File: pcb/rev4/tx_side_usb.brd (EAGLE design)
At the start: 28 x 36.5 mm, 55 parts, among them Q1 BSS84, U3 MCP73831T-2ACI/OT, Y1 CRYSTAL-26MHZSMD-3.2X2.5

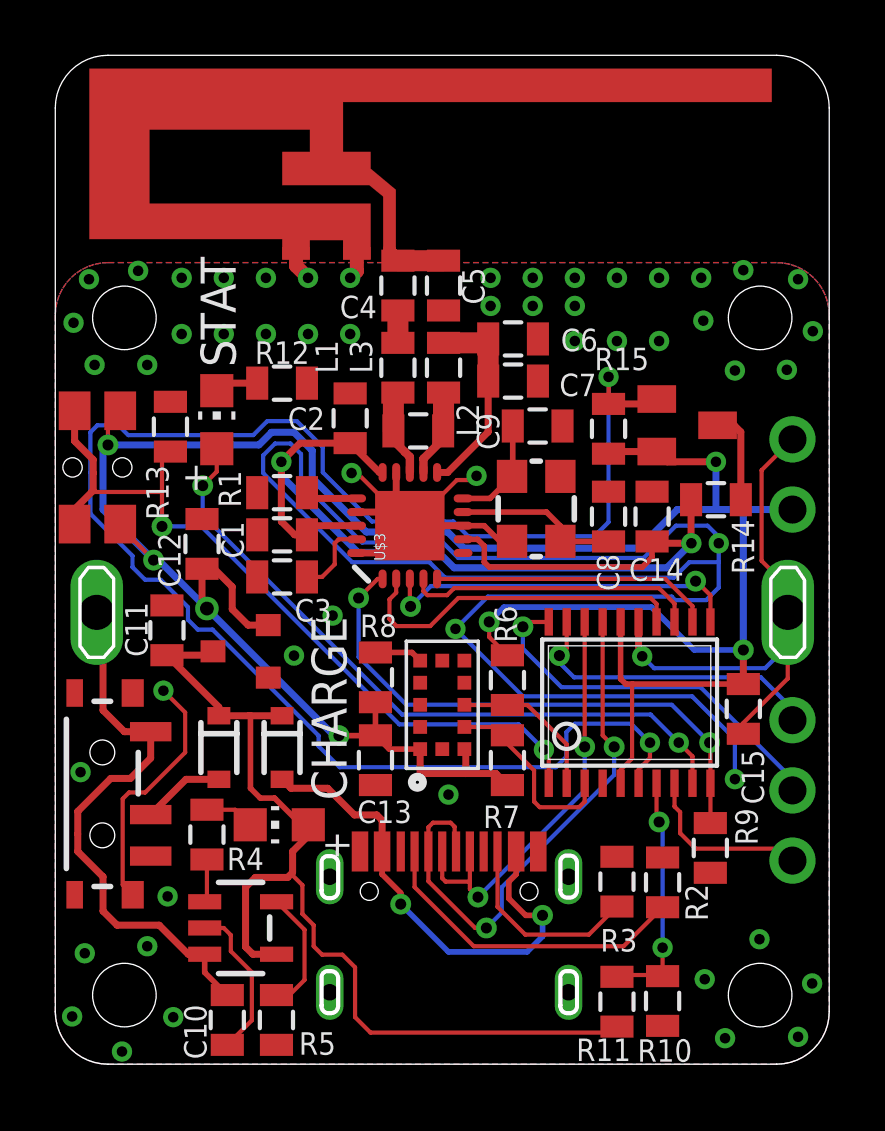
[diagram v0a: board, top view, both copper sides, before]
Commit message: added mounting hole plating
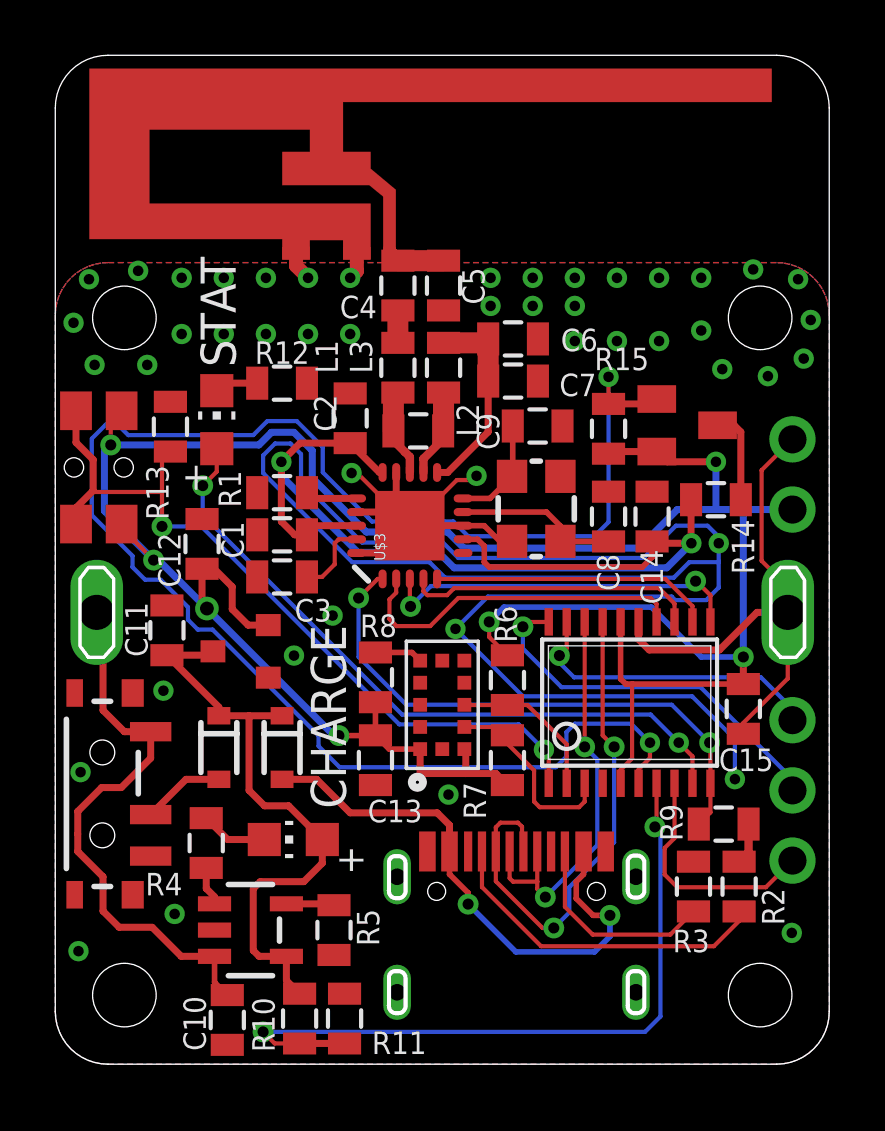
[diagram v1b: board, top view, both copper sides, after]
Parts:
- moved R11 11.5 mm to (10.5, 1.65), turned to 270 degrees
- moved R10 11.5 mm to (8.84, 1.65), turned to 90 degrees
- moved R5 3.86 mm to (10.1, 4.85)
- moved R3 2.77 mm to (23.1, 6.43)
- moved R2 2.77 mm to (24.7, 6.43)
- moved U$4 2.44 mm to (13.5, 7.70)
- moved R9 0.99 mm to (24.2, 8.69), turned to 0 degrees
- moved LED1 0.74 mm to (8.61, 8.13)
- moved U3 0.36 mm to (7.06, 4.85)
- moved R4 0.31 mm to (5.46, 8.00)
- moved U$10 0.05 mm to (1.57, 21.6)
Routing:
- net N$35: track 8.75 -> 26.3 mm
- net GND: track 116.2 -> 101.3 mm, vias 55 -> 47
- net N$27: track 36.1 -> 22.1 mm
- net N$17: track 4.49 -> 1.74 mm
- net N$26: track 17.7 -> 20.0 mm
- net N$33: track 6.37 -> 8.66 mm
- net N$34: track 19.9 -> 18.9 mm
- net N$18: track 15.3 -> 14.7 mm
- net N$12: track 1.79 -> 2.42 mm
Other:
- board text added: "CH"
- board text added: "DFU"
- board text added: "REV4 MAR19"
- board text removed: "CAL"
- board text removed: "REV4 MAR2 19"
